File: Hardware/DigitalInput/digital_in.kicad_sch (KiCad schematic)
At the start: 88 parts, among them Q1 SI2347DS, Q2 SI2347DS, Q3 SI2347DS, Q4 SI2347DS, Q5 SI2347DS, Q6 SI2347DS, Q7 SI2347DS, Q8 SI2347DS, U1 CNY17-3, U2 CNY17-3, U3 CNY17-3, U4 CNY17-3, U5 CNY17-3, U6 CNY17-3, U7 CNY17-3, U8 CNY17-3

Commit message: digital output & digital input update
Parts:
- removed C10, C11, C12, C13, C14, C15, C16, C9: 470p, Capacitor_SMD:C_0603_1608Metric_Pad1.08x0.95mm_HandSolder, symbol Device:C_Small
- removed R17, R18, R19, R20, R21, R22, R23, R24: 270k, Resistor_SMD:R_0603_1608Metric_Pad0.98x0.95mm_HandSolder, symbol Device:R_Small
- removed U1, U2, U3, U4, U5, U6, U7, U8: CNY17-3, PLC_STM:SOP254P1016X400-6N, symbol Isolator:CNY17-3
- added U1, U2, U3, U4, U5, U6, U7, U8: VO615A-3, Package_DIP:DIP-4_W8.89mm_SMDSocket_LongPads, symbol Isolator:VO615A-3
- D10: value LD_DI -> LD_DI1
- D11: value LD_DI -> LD_DI2
- D12: value LD_DI -> LD_DI3
- D13: value LD_DI -> LD_DI4
- D14: value LD_DI -> LD_DI5
- D15: value LD_DI -> LD_DI6
- D16: value LD_DI -> LD_DI7
- D9: value LD_DI -> LD_DI0
- renumbered R26 to R17, R27 to R18, R28 to R19, R29 to R20, R30 to R21, R31 to R22, R32 to R23, R33 to R24, R34 to R26, R35 to R27, R36 to R28, R37 to R29, R38 to R30, R39 to R31, R40 to R32
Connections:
- net GNDREF: now also U1.2, U2.2, U3.2, U4.2, U5.2, U6.2, U7.2, U8.2
- net OPT4_IN: now reaches C4.2, R12.2
- net OPT4_IN: now also U4.1
- net Q5_G: now reaches D5.2 (A), Q5.2 (G), R5.2
- net OPT7_IN: now reaches C7.2, R15.2
- net OPT7_IN: now also U7.1
- net OPT7_OUT: now reaches R23.1
- net OPT7_OUT: now also U7.4
- net OPT5_IN: now reaches C5.2, R13.2
- net OPT5_IN: now also U5.1
- net Q8_S: now reaches D8.1 (K), Q8.3 (S), R16.1
- net OPT8_IN: now reaches C8.2, R16.2
- net OPT8_IN: now also U8.1
- net Q6_G: now reaches D6.2 (A), Q6.2 (G), R6.2
- net OPT4_OUT: now reaches R20.1
- net OPT4_OUT: now also U4.4
- net OPT3_IN: now reaches C3.2, R11.2
- net OPT3_IN: now also U3.1
- net Q7_S: now reaches D7.1 (K), Q7.3 (S), R15.1
- net OPT8_OUT: now reaches R24.1
- net OPT8_OUT: now also U8.4
- net DI_4_R: now reaches D12.2 (A), R28.2
- net DI_1_R: now reaches D15.2 (A), R31.2
- net Q7_G: now reaches D7.2 (A), Q7.2 (G), R7.2
- net Q1_G: now reaches D1.2 (A), Q1.2 (G), R1.2
- net DI_0_R: now reaches D16.2 (A), R32.2
- net Q1_S: now reaches D1.1 (K), Q1.3 (S), R9.1
- net Q3_G: now reaches D3.2 (A), Q3.2 (G), R3.2
- net Q8_G: now reaches D8.2 (A), Q8.2 (G), R8.2
- net Q4_S: now reaches D4.1 (K), Q4.3 (S), R12.1
- net Q4_G: now reaches D4.2 (A), Q4.2 (G), R4.2
- net Q2_G: now reaches D2.2 (A), Q2.2 (G), R2.2
- net Q2_S: now reaches D2.1 (K), Q2.3 (S), R10.1
- net OPT1_OUT: now reaches R17.1
- net OPT1_OUT: now also U1.4
- net DI_3_R: now reaches D13.2 (A), R29.2
- net Q3_S: now reaches D3.1 (K), Q3.3 (S), R11.1
- net OPT5_OUT: now reaches R21.1
- net OPT5_OUT: now also U5.4
- net OPT6_OUT: now reaches R22.1
- net OPT6_OUT: now also U6.4
- net OPT2_IN: now reaches C2.2, R10.2
- net OPT2_IN: now also U2.1
- net DI_7_R: now reaches D9.2 (A), R25.2
- net Q5_S: now reaches D5.1 (K), Q5.3 (S), R13.1
- net OPT1_IN: now reaches C1.2, R9.2
- net OPT1_IN: now also U1.1
- net DI_5_R: now reaches D11.2 (A), R27.2
- net OPT2_OUT: now reaches R18.1
- net OPT2_OUT: now also U2.4
- net Q6_S: now reaches D6.1 (K), Q6.3 (S), R14.1
- net OPT6_IN: now reaches C6.2, R14.2
- net OPT6_IN: now also U6.1
- net OPT3_OUT: now reaches R19.1
- net OPT3_OUT: now also U3.4
- net DI_6_R: now reaches D10.2 (A), R26.2
- net DI_2_R: now reaches D14.2 (A), R30.2
- net DI0 renamed DI_0
- net DI_0: now also U1.3
- net DI1 renamed DI_1
- net DI_1: now also U2.3
- net DI2 renamed DI_2
- net DI_2: now also U3.3
- net DI3 renamed DI_3
- net DI_3: now also U4.3
- net DI4 renamed DI_4
- net DI_4: now also U5.3
- net DI5 renamed DI_5
- net DI_5: now also U6.3
- net DI6 renamed DI_6
- net DI_6: now also U7.3
- net DI7 renamed DI_7
- net DI_7: now also U8.3
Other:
- moved on the sheet: D10, D11, D12, D13, D14, D15, D16, R17, R18, R19, R20, R21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

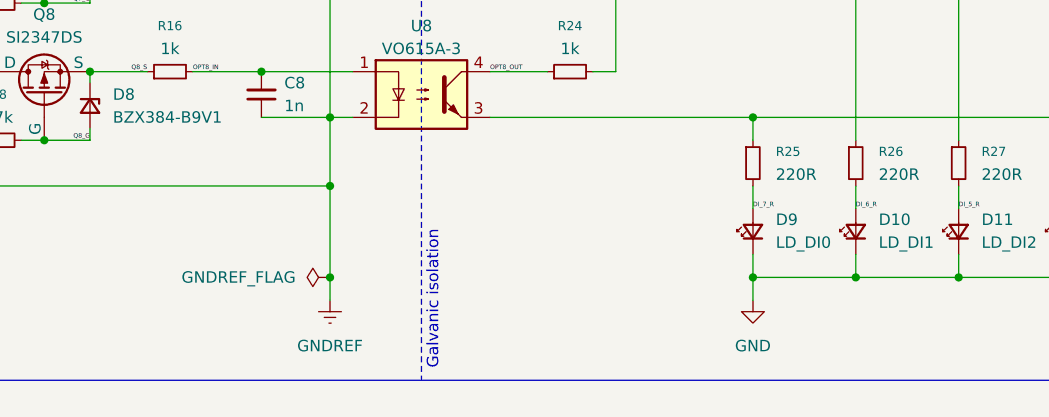
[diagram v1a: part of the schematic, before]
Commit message: digital input finished
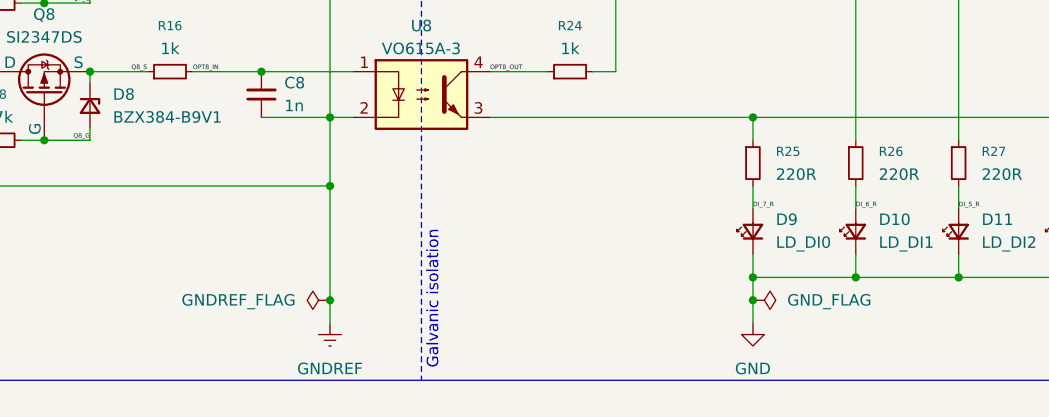
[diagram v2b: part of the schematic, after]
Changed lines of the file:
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@@
 	)
 	(junction
+		(at 166.37 154.94)
+		(diameter 0)
+		(color 0 0 0 0)
+	)
+	(junction
 		(at 212.09 73.66)
 		(diameter 0)
@@
 	)
 	(junction
-		(at 119.38 152.4)
-		(diameter 0)
-		(color 0 0 0 0)
-	)
-	(junction
 		(at 111.76 68.58)
 		(diameter 0)
@@
 	)
 	(junction
+		(at 119.38 154.94)
+		(diameter 0)
+		(color 0 0 0 0)
+	)
+	(junction
 		(at 177.8 152.4)
 		(diameter 0)
@@
 	(wire
 		(pts
+			(xy 166.37 154.94) (xy 166.37 157.48)
+		)
+		(stroke
+			(width 0)
+			(type default)
+		)
+	)
+	(wire
+		(pts
 			(xy 111.76 83.82) (xy 121.92 83.82)
 		)
@@
 	(wire
 		(pts
-			(xy 119.38 152.4) (xy 119.38 154.94)
+			(xy 119.38 142.24) (xy 119.38 154.94)
 		)
 		(stroke
@@
 	(wire
 		(pts
-			(xy 119.38 142.24) (xy 119.38 152.4)
-		)
-		(stroke
-			(width 0)
-			(type default)
-		)
-	)
-	(wire
-		(pts
 			(xy 137.16 22.86) (xy 143.51 22.86)
 		)
@@
 	(wire
 		(pts
+			(xy 119.38 154.94) (xy 119.38 157.48)
+		)
+		(stroke
+			(width 0)
+			(type default)
+		)
+	)
+	(wire
+		(pts
 			(xy 111.76 58.42) (xy 119.38 58.42)
 		)
@@
 	(symbol
 		(lib_id "power:GND")
-		(at 166.37 154.94 0)
+		(at 166.37 157.48 0)
 		(unit 1)
 		(exclude_from_sim no)
@@
 		(fields_autoplaced yes)
 		(property "Reference" "#PWR03"
-			(at 166.37 161.29 0)
+			(at 166.37 163.83 0)
 			(effects
 				(font
@@
 		)
 		(property "Value" "GND"
-			(at 166.37 160.02 0)
+			(at 166.37 162.56 0)
 			(effects
 				(font
@@
 		)
 		(property "Footprint" ""
-			(at 166.37 154.94 0)
+			(at 166.37 157.48 0)
 			(effects
 				(font
@@
 		)
 		(property "Datasheet" ""
-			(at 166.37 154.94 0)
+			(at 166.37 157.48 0)
 			(effects
 				(font
@@
 		)
 		(property "Description" "Power symbol creates a global label with name \"GND\" , ground"
-			(at 166.37 154.94 0)
+			(at 166.37 157.48 0)
 			(effects
 				(font
@@
 	(symbol
 		(lib_id "power:GNDREF")
-		(at 119.38 154.94 0)
+		(at 119.38 157.48 0)
 		(unit 1)
 		(exclude_from_sim no)
@@
 		(fields_autoplaced yes)
 		(property "Reference" "#PWR01"
-			(at 119.38 161.29 0)
+			(at 119.38 163.83 0)
 			(effects
 				(font
@@
 		)
 		(property "Value" "GNDREF"
-			(at 119.38 160.02 0)
+			(at 119.38 162.56 0)
 			(effects
 				(font
@@
 		)
 		(property "Footprint" ""
-			(at 119.38 154.94 0)
+			(at 119.38 157.48 0)
 			(effects
 				(font
@@
 		)
 		(property "Datasheet" ""
-			(at 119.38 154.94 0)
+			(at 119.38 157.48 0)
 			(effects
 				(font
@@
 		)
 		(property "Description" "Power symbol creates a global label with name \"GNDREF\" , reference supply ground"
-			(at 119.38 154.94 0)
+			(at 119.38 157.48 0)
 			(effects
 				(font
@@
 	(symbol
 		(lib_id "power:PWR_FLAG")
-		(at 119.38 152.4 90)
+		(at 119.38 154.94 90)
 		(mirror x)
 		(unit 1)
@@
 		(dnp no)
 		(property "Reference" "#FLG01"
-			(at 117.475 152.4 0)
+			(at 117.475 154.94 0)
 			(effects
 				(font
@@
 		)
 		(property "Value" "GNDREF_FLAG"
-			(at 115.57 152.3999 90)
+			(at 115.57 154.9399 90)
 			(effects
 				(font
@@
 		)
 		(property "Footprint" ""
-			(at 119.38 152.4 0)
+			(at 119.38 154.94 0)
 			(effects
 				(font
@@
 		)
 		(property "Datasheet" "~"
-			(at 119.38 152.4 0)
+			(at 119.38 154.94 0)
 			(effects
 				(font
@@
 		)
 		(property "Description" "Special symbol for telling ERC where power comes from"
-			(at 119.38 152.4 0)
+			(at 119.38 154.94 0)
 			(effects
 				(font
@@
 					(unit 1)
 				)
+			)
+		)
+	)
+	(symbol
+		(lib_id "power:PWR_FLAG")
+		(at 166.37 154.94 270)
+		(mirror x)
+		(unit 1)
+		(exclude_from_sim no)
+		(in_bom yes)
+		(on_board yes)
+		(dnp no)
+		(property "Reference" "#FLG03"
+			(at 168.275 154.94 0)
+			(effects
+				(font
+					(size 1.27 1.27)
+				)
+				(hide yes)
+			)
+		)
+		(property "Value" "GND_FLAG"
+			(at 170.18 154.9401 90)
+			(effects
+				(font
+					(size 1.27 1.27)
+				)
+				(justify left)
+			)
+		)
+		(property "Footprint" ""
+			(at 166.37 154.94 0)
+			(effects
+				(font
+					(size 1.27 1.27)
+				)
+				(hide yes)
+			)
+		)
+		(property "Datasheet" "~"
+			(at 166.37 154.94 0)
+			(effects
+				(font
+					(size 1.27 1.27)
+				)
+				(hide yes)
+			)
+		)
+		(property "Description" "Special symbol for telling ERC where power comes from"
+			(at 166.37 154.94 0)
+			(effects
+				(font
+					(size 1.27 1.27)
+				)
+				(hide yes)
+			)
+		)
+		(pin "1"
+		)
+		(instances
+			(project "digital_input"
+				(path "/b652b05a-4e3d-4ad1-b032-18886abe7d45/6a3b3241-0ad0-4b16-a514-26e740810b1b"
+					(reference "#FLG03")
+					(unit 1)
+				)

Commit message: small adjustments
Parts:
- U1, U2, U3, U4, U5, U6, U7, U8: Mouser Part Number (none) -> 78-VO615A-3X007T; Mouser Price/Stock (none) -> https://www.mouser.pl/ProductDetail/Vishay-Semiconductors/V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
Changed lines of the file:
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@@
 			)
 		)
+		(property "Mouser Part Number" "78-VO615A-3X007T"
+			(at 129.54 116.84 0)
+			(effects
+				(font
+					(size 1.27 1.27)
+				)
+				(hide yes)
+			)
+		)
+		(property "Mouser Price/Stock" "https://www.mouser.pl/ProductDetail/Vishay-Semiconductors/VO615A-3X007T?qs=zUyzn9J%252BIQpvF7TWq5It%252BA%3D%3D"
+			(at 129.54 116.84 0)
+			(effects
+				(font
+					(size 1.27 1.27)
+				)
+				(hide yes)
+			)
+		)
 		(pin "2"
 		)
@@
 			)
 		)
+		(property "Mouser Part Number" "78-VO615A-3X007T"
+			(at 129.54 101.6 0)
+			(effects
+				(font
+					(size 1.27 1.27)
+				)
+				(hide yes)
+			)
+		)
+		(property "Mouser Price/Stock" "https://www.mouser.pl/ProductDetail/Vishay-Semiconductors/VO615A-3X007T?qs=zUyzn9J%252BIQpvF7TWq5It%252BA%3D%3D"
+			(at 129.54 101.6 0)
+			(effects
+				(font
+					(size 1.27 1.27)
+				)
+				(hide yes)
+			)
+		)
 		(pin "2"
 		)
@@
 			)
 		)
+		(property "Mouser Part Number" "78-VO615A-3X007T"
+			(at 129.54 40.64 0)
+			(effects
+				(font
+					(size 1.27 1.27)
+				)
+				(hide yes)
+			)
+		)
+		(property "Mouser Price/Stock" "https://www.mouser.pl/ProductDetail/Vishay-Semiconductors/VO615A-3X007T?qs=zUyzn9J%252BIQpvF7TWq5It%252BA%3D%3D"
+			(at 129.54 40.64 0)
+			(effects
+				(font
+					(size 1.27 1.27)
+				)
+				(hide yes)
+			)
+		)
 		(pin "2"
 		)
@@
 			)
 		)
+		(property "Mouser Part Number" "78-VO615A-3X007T"
+			(at 129.54 86.36 0)
+			(effects
+				(font
+					(size 1.27 1.27)
+				)
+				(hide yes)
+			)
+		)
+		(property "Mouser Price/Stock" "https://www.mouser.pl/ProductDetail/Vishay-Semiconductors/VO615A-3X007T?qs=zUyzn9J%252BIQpvF7TWq5It%252BA%3D%3D"
+			(at 129.54 86.36 0)
+			(effects
+				(font
+					(size 1.27 1.27)
+				)
+				(hide yes)
+			)
+		)
 		(pin "2"
 		)
@@
 			)
 		)
+		(property "Mouser Part Number" "78-VO615A-3X007T"
+			(at 129.54 25.4 0)
+			(effects
+				(font
+					(size 1.27 1.27)
+				)
+				(hide yes)
+			)
+		)
+		(property "Mouser Price/Stock" "https://www.mouser.pl/ProductDetail/Vishay-Semiconductors/VO615A-3X007T?qs=zUyzn9J%252BIQpvF7TWq5It%252BA%3D%3D"
+			(at 129.54 25.4 0)
+			(effects
+				(font
+					(size 1.27 1.27)
+				)
+				(hide yes)
+			)
+		)
 		(pin "2"
 		)
@@
 			)
 		)
+		(property "Mouser Part Number" "78-VO615A-3X007T"
+			(at 129.54 55.88 0)
+			(effects
+				(font
+					(size 1.27 1.27)
+				)
+				(hide yes)
+			)
+		)
+		(property "Mouser Price/Stock" "https://www.mouser.pl/ProductDetail/Vishay-Semiconductors/VO615A-3X007T?qs=zUyzn9J%252BIQpvF7TWq5It%252BA%3D%3D"
+			(at 129.54 55.88 0)
+			(effects
+				(font
+					(size 1.27 1.27)
+				)
+				(hide yes)
+			)
+		)
 		(pin "2"
 		)
@@
 			)
 		)
+		(property "Mouser Part Number" "78-VO615A-3X007T"
+			(at 129.54 132.08 0)
+			(effects
+				(font
+					(size 1.27 1.27)
+				)
+				(hide yes)
+			)
+		)
+		(property "Mouser Price/Stock" "https://www.mouser.pl/ProductDetail/Vishay-Semiconductors/VO615A-3X007T?qs=zUyzn9J%252BIQpvF7TWq5It%252BA%3D%3D"
+			(at 129.54 132.08 0)
+			(effects
+				(font
+					(size 1.27 1.27)
+				)
+				(hide yes)
+			)
+		)
 		(pin "2"
 		)
@@
 			(at 129.54 71.12 0)
 			(effects
+				(font
+					(size 1.27 1.27)
+				)
+				(hide yes)
+			)
+		)
+		(property "Mouser Part Number" "78-VO615A-3X007T"
+			(at 129.54 71.12 0)
+			(effects
+				(font
+					(size 1.27 1.27)
+				)
+				(hide yes)
+			)
+		)
+		(property "Mouser Price/Stock" "https://www.mouser.pl/ProductDetail/Vishay-Semiconductors/VO615A-3X007T?qs=zUyzn9J%252BIQpvF7TWq5It%252BA%3D%3D"
+			(at 129.54 71.12 0)
+			(effects
